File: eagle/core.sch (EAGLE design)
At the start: 48 parts, among them IC5 APX803, T1 BC846, T2 BC846, T3 BC846, T4 BC846

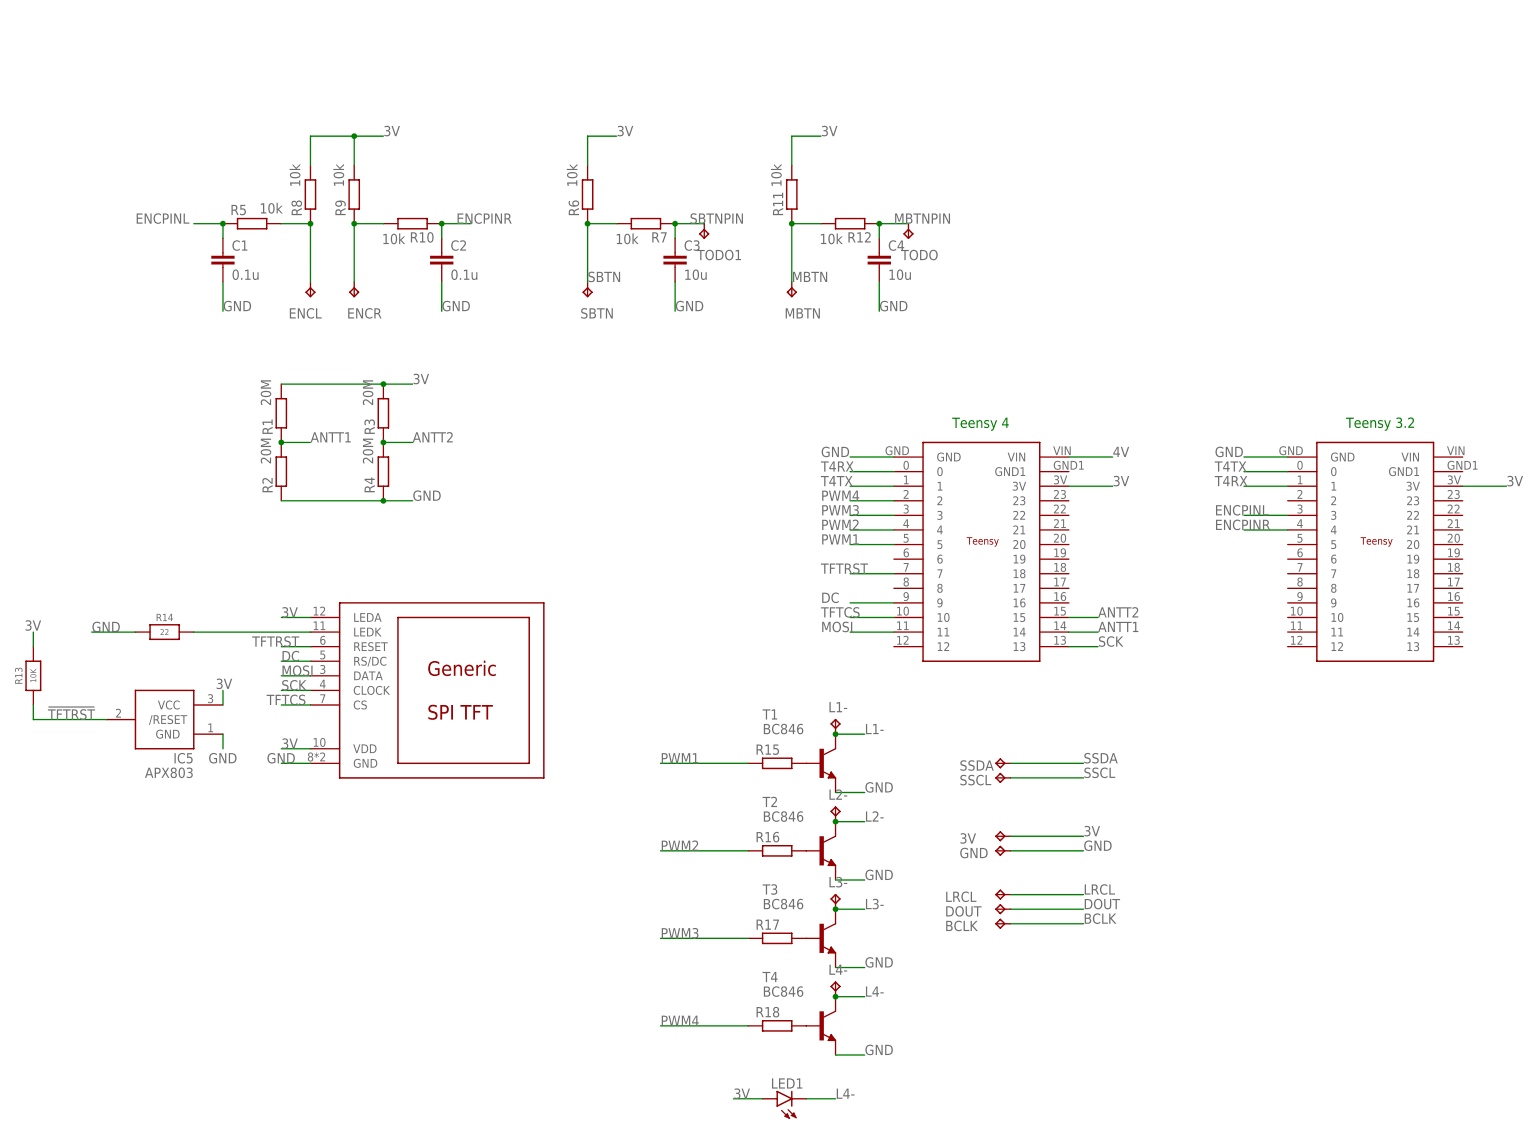
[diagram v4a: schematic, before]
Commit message: decided on ffc wire layout.
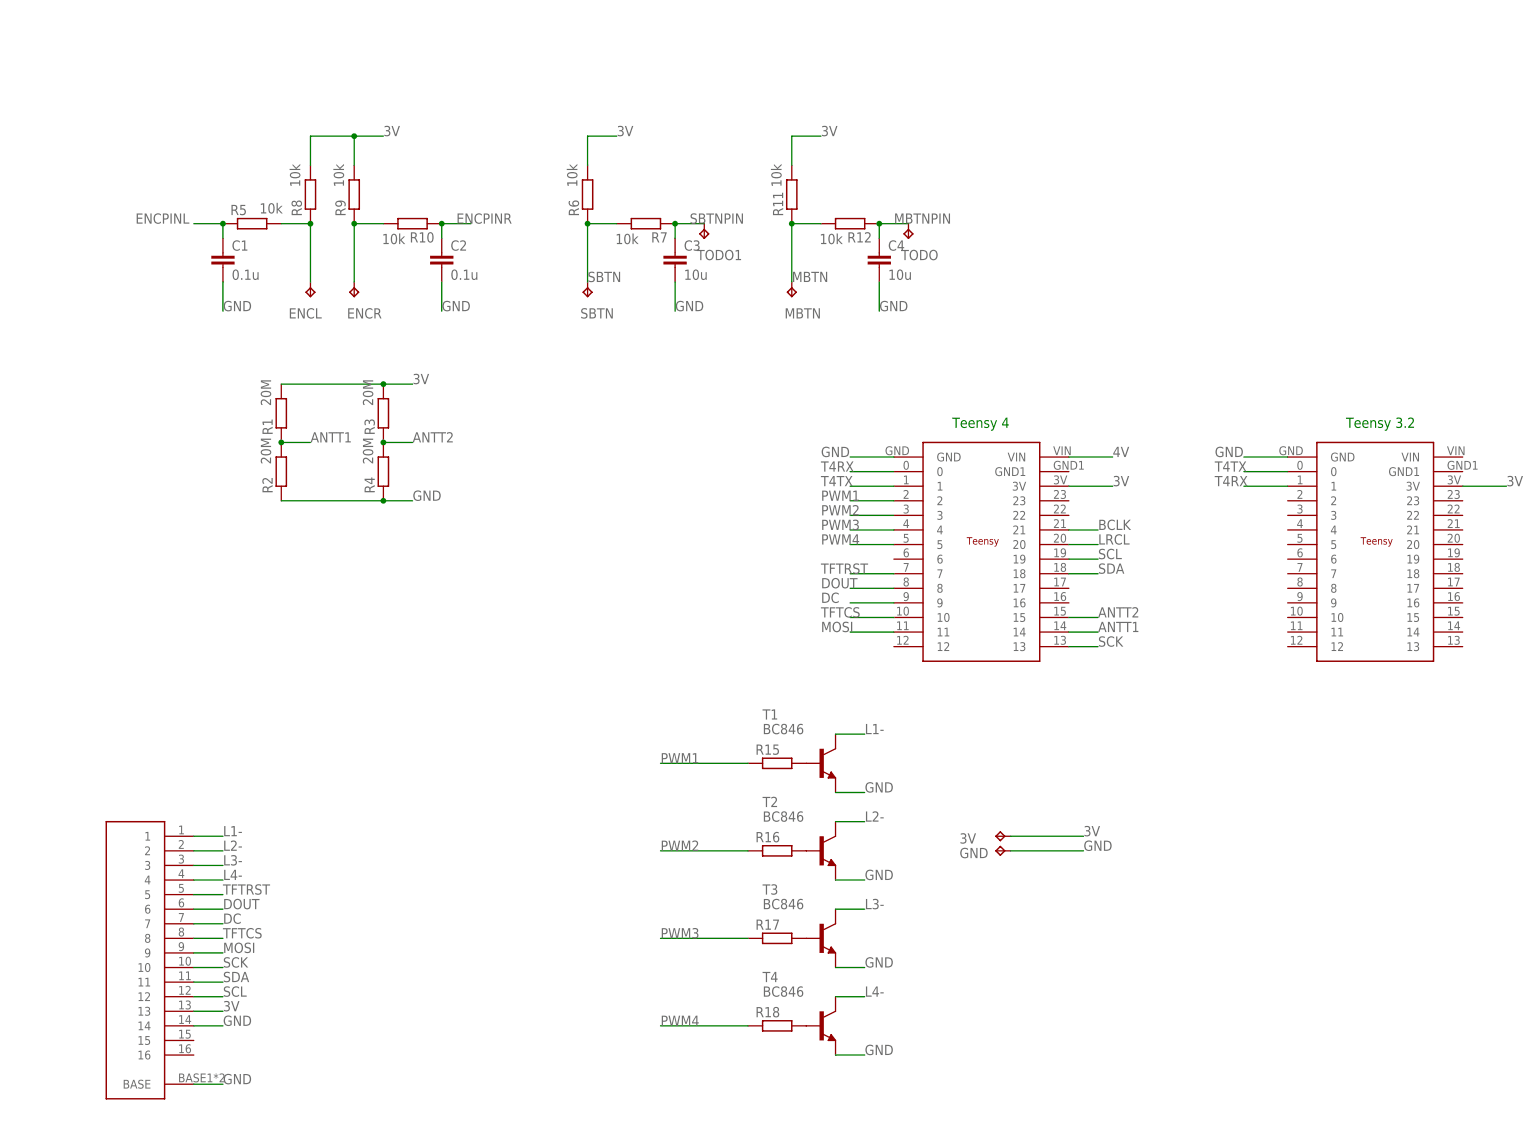
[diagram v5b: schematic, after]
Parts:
- removed BCLK, DOUT, L1-, L2-, L3-, L4-, LRCL, SSCL, SSDA: TPTP16R, testpad:TPTP16R
- removed IC5: APX803, adafruit:AXP083-SAG
- removed LED1: (no value), led:LED3MM
- removed R13: 10K, microbuilder:RESISTOR_0603_NOOUT
- removed R14: 22, microbuilder:RESISTOR_0603_NOOUT
- removed U$4: TFT, general:TFT
- added U$3: 16PINFFC, general:16PINFFC
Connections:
- removed net !TFTRST: IC5./RESET, R13.1
- removed net N$1: R14.2, U$4.LEDK
- removed net SSCL: SSCL.TP
- removed net SSDA: SSDA.TP
- new net SCL: U$1.19, U$3.12
- new net SDA: U$1.18, U$3.11
- net 3V: now also U$3.13; no longer IC5.VCC, LED1.A, R13.2, U$4.LEDA, U$4.VDD
- net BCLK: now also U$1.21; no longer BCLK.TP
- net DC: now also U$3.7; no longer U$4.RS/DC
- net DOUT: now also U$1.8, U$3.6; no longer DOUT.TP
- net ENCPINL: no longer U$2.3
- net ENCPINR: no longer U$2.4
- net GND: now also U$3.14, U$3.BASE; no longer IC5.GND, R14.1, U$4.GND
- net L1-: now also U$3.1; no longer L1-.TP
- net L2-: now also U$3.2; no longer L2-.TP
- net L3-: now also U$3.3; no longer L3-.TP
- net L4-: now also U$3.4; no longer L4-.TP, LED1.C
- net LRCL: now also U$1.20; no longer LRCL.TP
- net MOSI: now also U$3.9; no longer U$4.DATA
- net PWM1: now also U$1.2; no longer U$1.5
- net PWM2: now also U$1.3; no longer U$1.4
- net PWM3: now also U$1.4; no longer U$1.3
- net PWM4: now also U$1.5; no longer U$1.2
- net SCK: now also U$3.10; no longer U$4.CLOCK
- net TFTCS: now also U$3.8; no longer U$4.CS
- net TFTRST: now also U$3.5; no longer U$4.RESET

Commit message: First order of probe, probebase and FFC breakout PCBs for 22mm enclosure
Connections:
- net 3V: now also U$3.15; no longer U$3.13
- net BCLK: now also U$3.14
- net GND: now also U$3.16; no longer U$3.14
- net LRCL: now also U$3.13
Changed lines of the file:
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@@
-</segment>
-<segment>
-<pinref part="U$3" gate="G$1" pin="14"/>
-<wire x1="-180.34" y1="-20.32" x2="-175.26" y2="-20.32" width="0.1524" layer="91"/>
-<label x="-175.26" y="-20.32" size="1.778" layer="95"/>
 </segment>
 <segment>
@@
 <wire x1="-180.34" y1="-30.48" x2="-175.26" y2="-30.48" width="0.1524" layer="91"/>
 <label x="-175.26" y="-30.48" size="1.778" layer="95"/>
+</segment>
+<segment>
+<pinref part="U$3" gate="G$1" pin="16"/>
+<wire x1="-180.34" y1="-25.4" x2="-175.26" y2="-25.4" width="0.1524" layer="91"/>
+<label x="-175.26" y="-25.4" size="1.778" layer="95"/>
 </segment>
 </net>
@@
 </segment>
 <segment>
-<pinref part="U$3" gate="G$1" pin="13"/>
-<wire x1="-180.34" y1="-17.78" x2="-175.26" y2="-17.78" width="0.1524" layer="91"/>
-<label x="-175.26" y="-17.78" size="1.778" layer="95"/>
+<pinref part="U$3" gate="G$1" pin="15"/>
+<wire x1="-180.34" y1="-22.86" x2="-175.26" y2="-22.86" width="0.1524" layer="91"/>
+<label x="-175.26" y="-22.86" size="1.778" layer="95"/>
 </segment>
 </net>
@@
 <label x="-22.86" y="66.04" size="1.778" layer="95"/>
 </segment>
+<segment>
+<pinref part="U$3" gate="G$1" pin="14"/>
+<wire x1="-180.34" y1="-20.32" x2="-175.26" y2="-20.32" width="0.1524" layer="91"/>
+<label x="-175.26" y="-20.32" size="1.778" layer="95"/>
+</segment>
 </net>
 <net name="DOUT" class="0">
@@
 <label x="-22.86" y="63.5" size="1.778" layer="95"/>
 </segment>
-</net>
+<segment>
+<pinref part="U$3" gate="G$1" pin="13"/>
+<wire x1="-180.34" y1="-17.78" x2="-175.26" y2="-17.78" width="0.1524" layer="91"/>
+<label x="-175.26" y="-17.78" size="1.778" layer="95"/>
+</segment>
+</net>

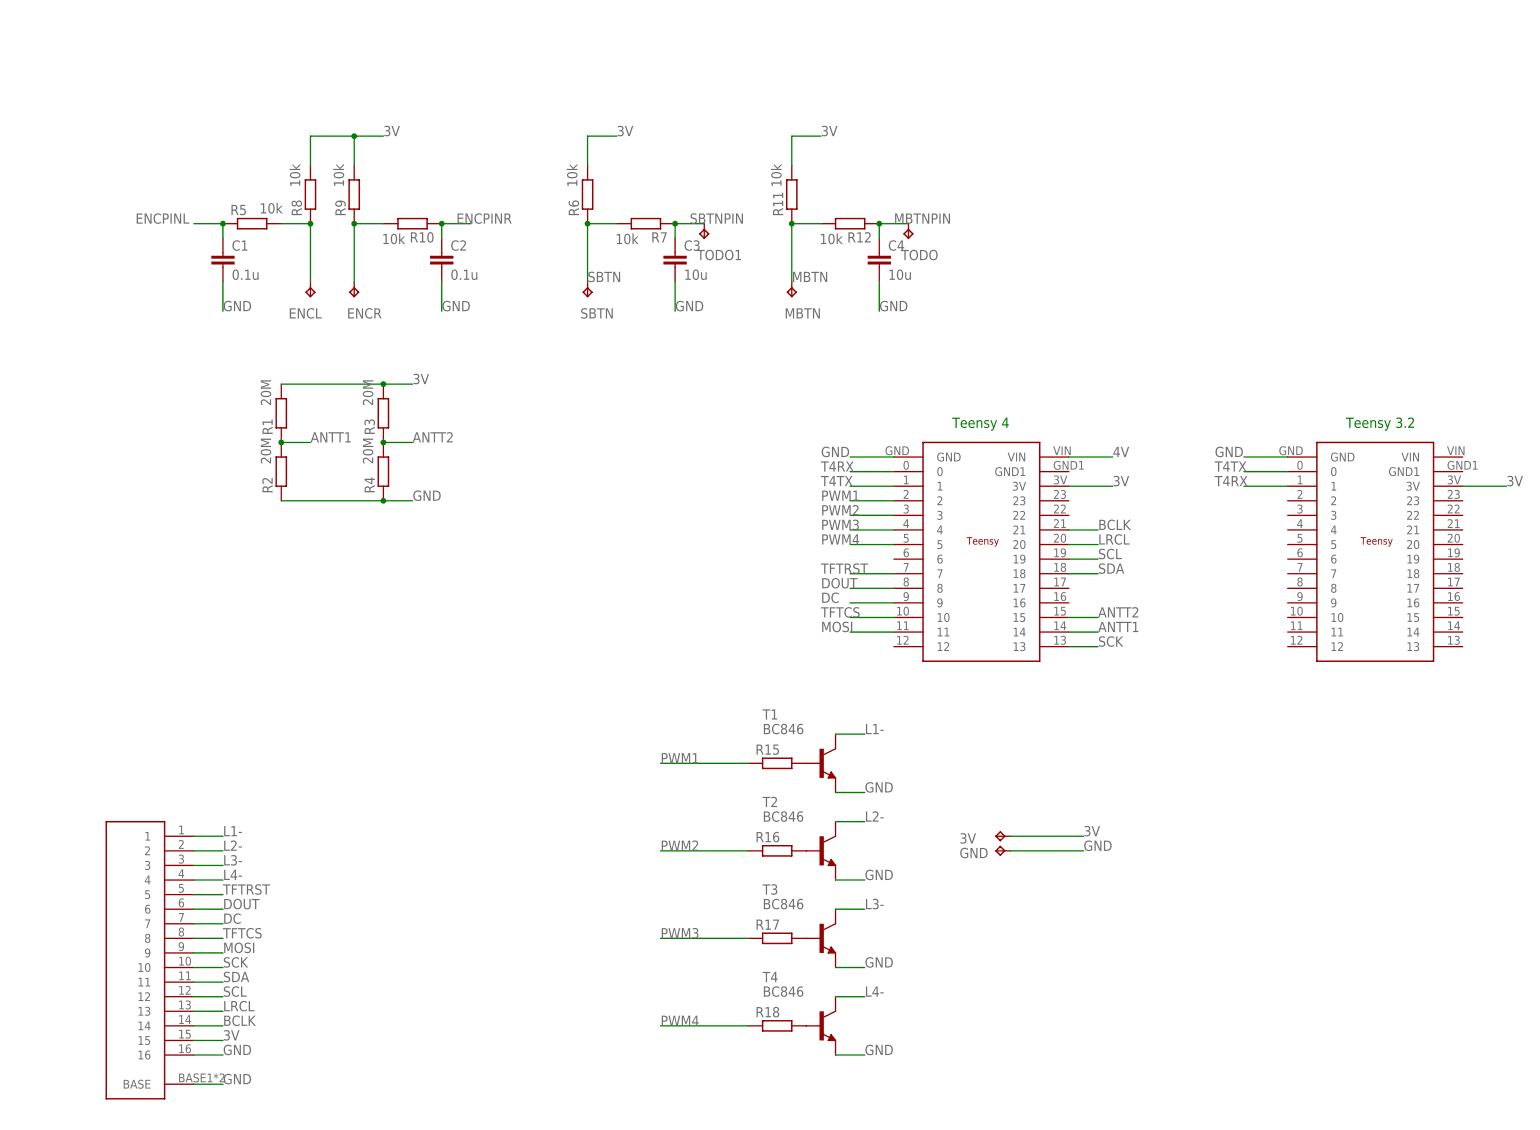
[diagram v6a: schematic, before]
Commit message: core pcb improvements
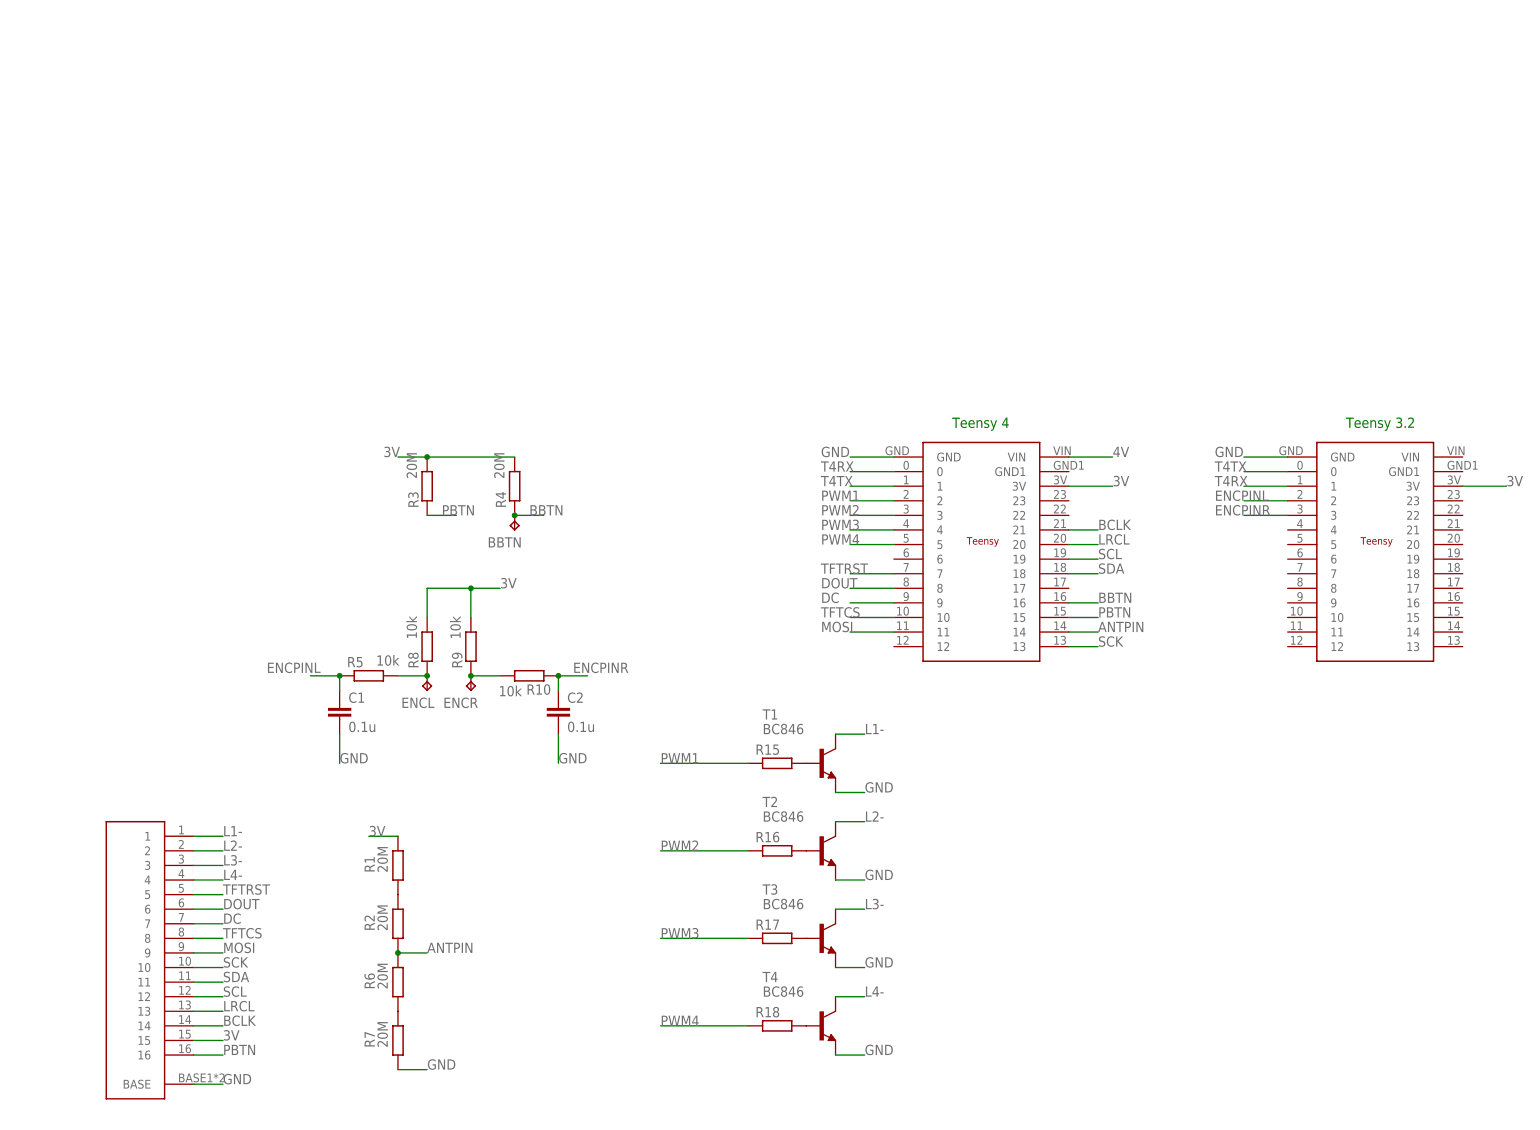
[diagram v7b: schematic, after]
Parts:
- removed 3V, GND: TPTP16R, testpad:TPTP16R
- removed C3, C4: 10u, resistor:C-EUC0805
- removed MBTN, SBTN, TODO, TODO1: TPTP10R, testpad:TPTP10R
- removed R11, R12: 10k, resistor:R-EU_M0805
- added BBTN: TPTP14R, testpad:TPTP14R
- ENCL, ENCR: value TPTP10R -> TPTP14R; device testpad:TPTP10R -> testpad:TPTP14R
- R6, R7: value 10k -> 20M
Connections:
- removed net ANTT1: R1.1, R2.2, U$1.14
- removed net ANTT2: R3.1, R4.2, U$1.15
- removed net MBTN: MBTN.TP, R11.1, R12.2
- removed net MBTNPIN: C4.1, R12.1, TODO.TP
- removed net SBTN: R6.1, R7.2, SBTN.TP
- removed net SBTNPIN: C3.1, R7.1, TODO1.TP
- new net ANTPIN: R2.1, R6.2, U$1.14
- new net BBTN: BBTN.TP, R4.1, U$1.16
- new net N$6: R6.1, R7.2
- new net N$7: R1.1, R2.2
- new net PBTN: R3.1, U$1.15, U$3.16
- net 3V: now also R4.2; no longer 3V.TP, R11.2, R6.2
- net ENCPINL: now also U$2.2
- net ENCPINR: now also U$2.3
- net GND: now also R7.1; no longer C3.2, C4.2, GND.TP, R2.1, R4.1, U$3.16
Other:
- moved on the sheet: C1, C2, ENCL, ENCR, R1, R10, R2, R3, R4, R5, R6, R7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
